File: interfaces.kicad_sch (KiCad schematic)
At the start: 84 parts, among them IC1 TPD8S009DSMR, J1 WE_629105150521, J2 685119134923, J3 1140084168, Q1 BSS138APW, Q2 BSS138APW, Q3 BSS138APW, Q4 BSS138APW, Q5 BSS138APW, U4 FT4232H-56Q, Y1 ABM8G-12.000MHZ-18-D2Y-T

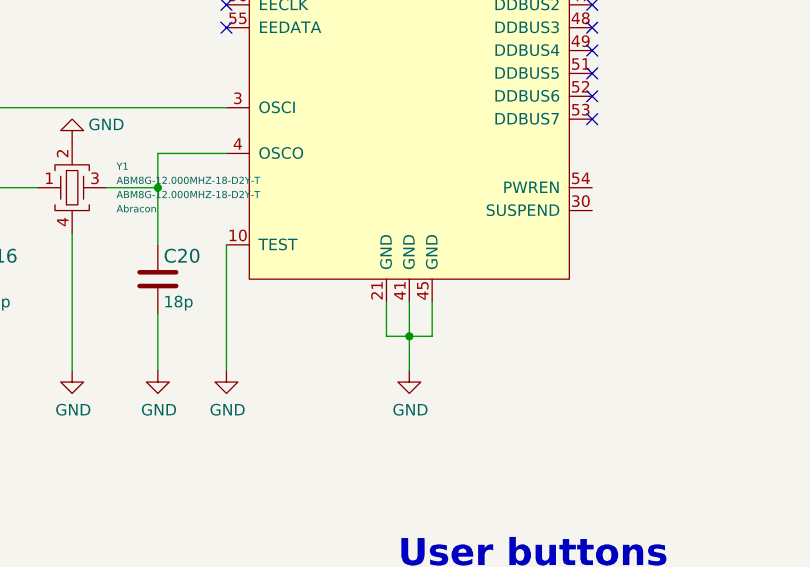
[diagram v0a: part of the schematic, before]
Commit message: Add 0.6V LDO as an option, fix floating EP on FTDI, clean DRC
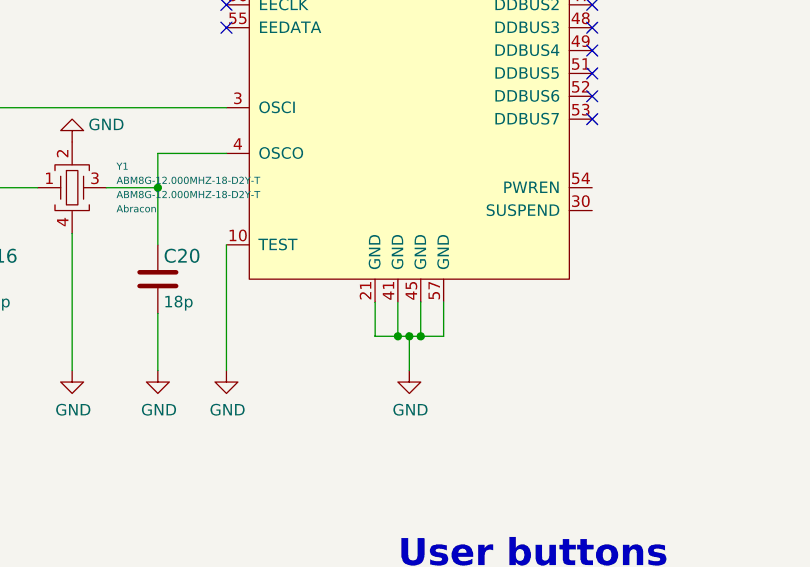
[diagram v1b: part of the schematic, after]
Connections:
- net GND: now also U4.57 (GND)
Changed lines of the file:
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@@
   (junction (at 345.44 70.485) (diameter 0) (color 0 0 0 0)
   )
+  (junction (at 111.76 182.88) (diameter 0) (color 0 0 0 0)
+  )
   (junction (at 301.625 158.75) (diameter 0) (color 0 0 0 0)
   )
@@
   (junction (at 83.82 86.36) (diameter 0) (color 0 0 0 0)
   )
-  (junction (at 110.49 182.88) (diameter 0) (color 0 0 0 0)
+  (junction (at 109.22 182.88) (diameter 0) (color 0 0 0 0)
   )
   (junction (at 294.005 158.75) (diameter 0) (color 0 0 0 0)
@@
   (junction (at 87.63 76.2) (diameter 0) (color 0 0 0 0)
   )
+  (junction (at 110.49 182.88) (diameter 0) (color 0 0 0 0)
+  )
   (junction (at 44.45 215.265) (diameter 0) (color 0 0 0 0)
   )
@@
     (stroke (width 0) (type default) (color 0 0 0 0))
   )
-  (wire (pts (xy 110.49 179.07) (xy 110.49 182.88))
+  (wire (pts (xy 109.22 179.07) (xy 109.22 182.88))
     (stroke (width 0) (type default) (color 0 0 0 0))
   )
@@
     (stroke (width 0) (type default) (color 0 0 0 0))
   )
+  (wire (pts (xy 110.49 182.88) (xy 109.22 182.88))
+    (stroke (width 0) (type default) (color 0 0 0 0))
+  )
   (wire (pts (xy 278.13 69.215) (xy 280.67 69.215))
     (stroke (width 0) (type default) (color 0 0 0 0))
@@
     (stroke (width 0) (type default) (color 0 0 0 0))
   )
-  (wire (pts (xy 113.03 182.88) (xy 110.49 182.88))
+  (wire (pts (xy 114.3 179.07) (xy 114.3 182.88))
+    (stroke (width 0) (type default) (color 0 0 0 0))
+  )
+  (wire (pts (xy 111.76 182.88) (xy 110.49 182.88))
     (stroke (width 0) (type default) (color 0 0 0 0))
   )
@@
     (stroke (width 0) (type default) (color 0 0 0 0))
   )
-  (wire (pts (xy 113.03 179.07) (xy 113.03 182.88))
+  (wire (pts (xy 111.76 179.07) (xy 111.76 182.88))
     (stroke (width 0) (type default) (color 0 0 0 0))
   )
@@
     (stroke (width 0) (type default) (color 0 0 0 0))
   )
-  (wire (pts (xy 107.95 182.88) (xy 110.49 182.88))
+  (wire (pts (xy 106.68 182.88) (xy 109.22 182.88))
     (stroke (width 0) (type default) (color 0 0 0 0))
   )
@@
     (stroke (width 0) (type default) (color 0 0 0 0))
   )
-  (wire (pts (xy 107.95 179.07) (xy 107.95 182.88))
+  (wire (pts (xy 106.68 179.07) (xy 106.68 182.88))
     (stroke (width 0) (type default) (color 0 0 0 0))
   )
@@
     (stroke (width 0) (type default) (color 0 0 0 0))
   )
+  (wire (pts (xy 114.3 182.88) (xy 111.76 182.88))
+    (stroke (width 0) (type default) (color 0 0 0 0))
+  )
   (wire (pts (xy 90.17 101.6) (xy 87.63 101.6))
     (stroke (width 0) (type default) (color 0 0 0 0))
@@
     (pin "55")
     (pin "56")
+    (pin "57")
     (pin "6")
     (pin "7")
